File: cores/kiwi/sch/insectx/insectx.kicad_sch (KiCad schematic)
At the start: 0 parts

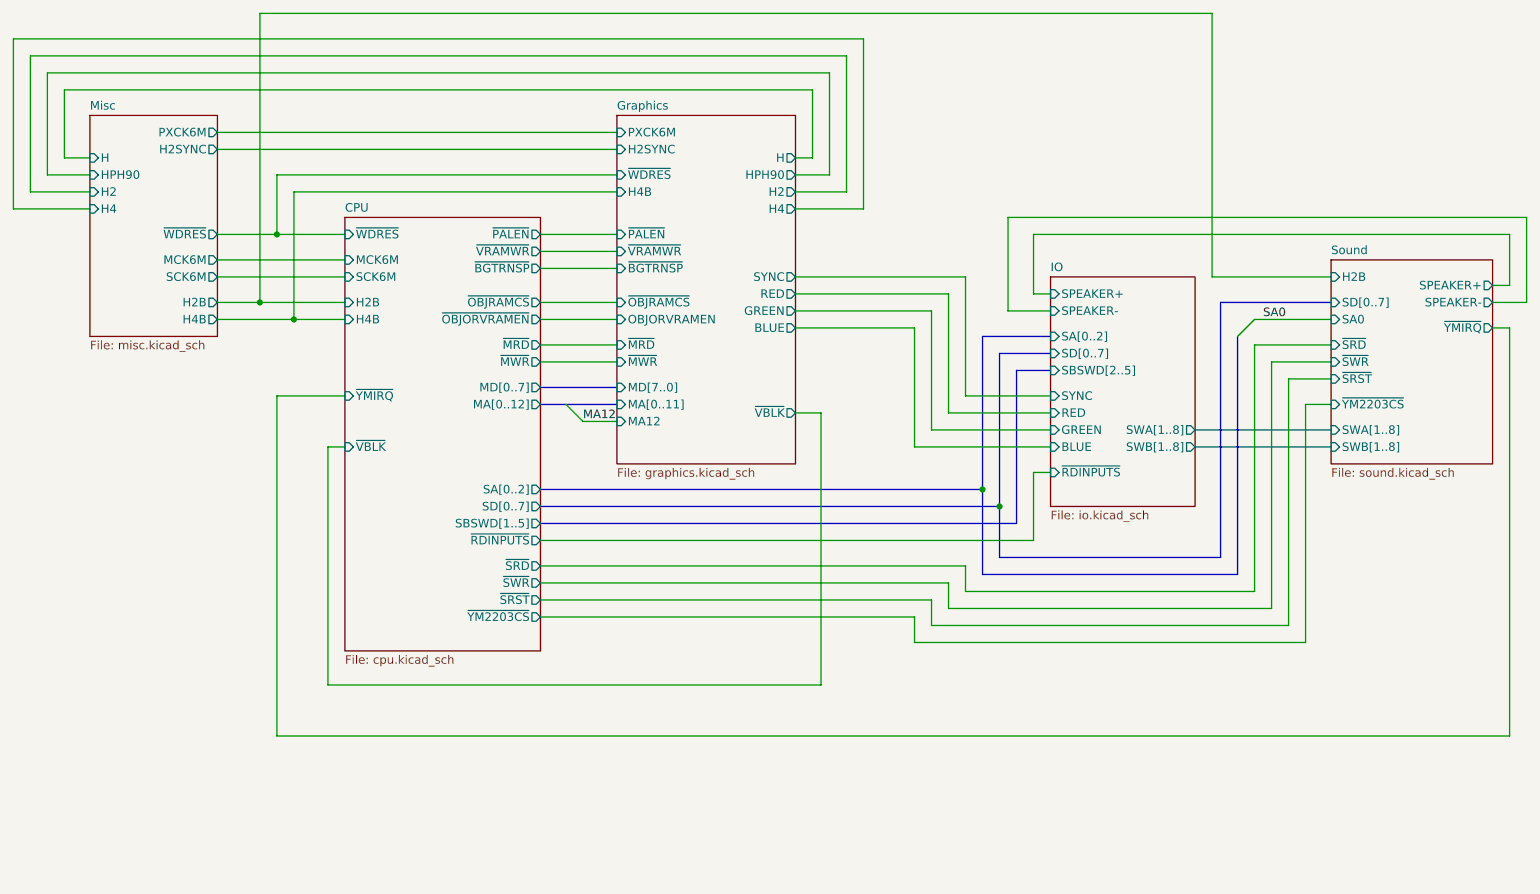
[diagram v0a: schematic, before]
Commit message: Updated schematics according to: [insectx] schematic signals #22
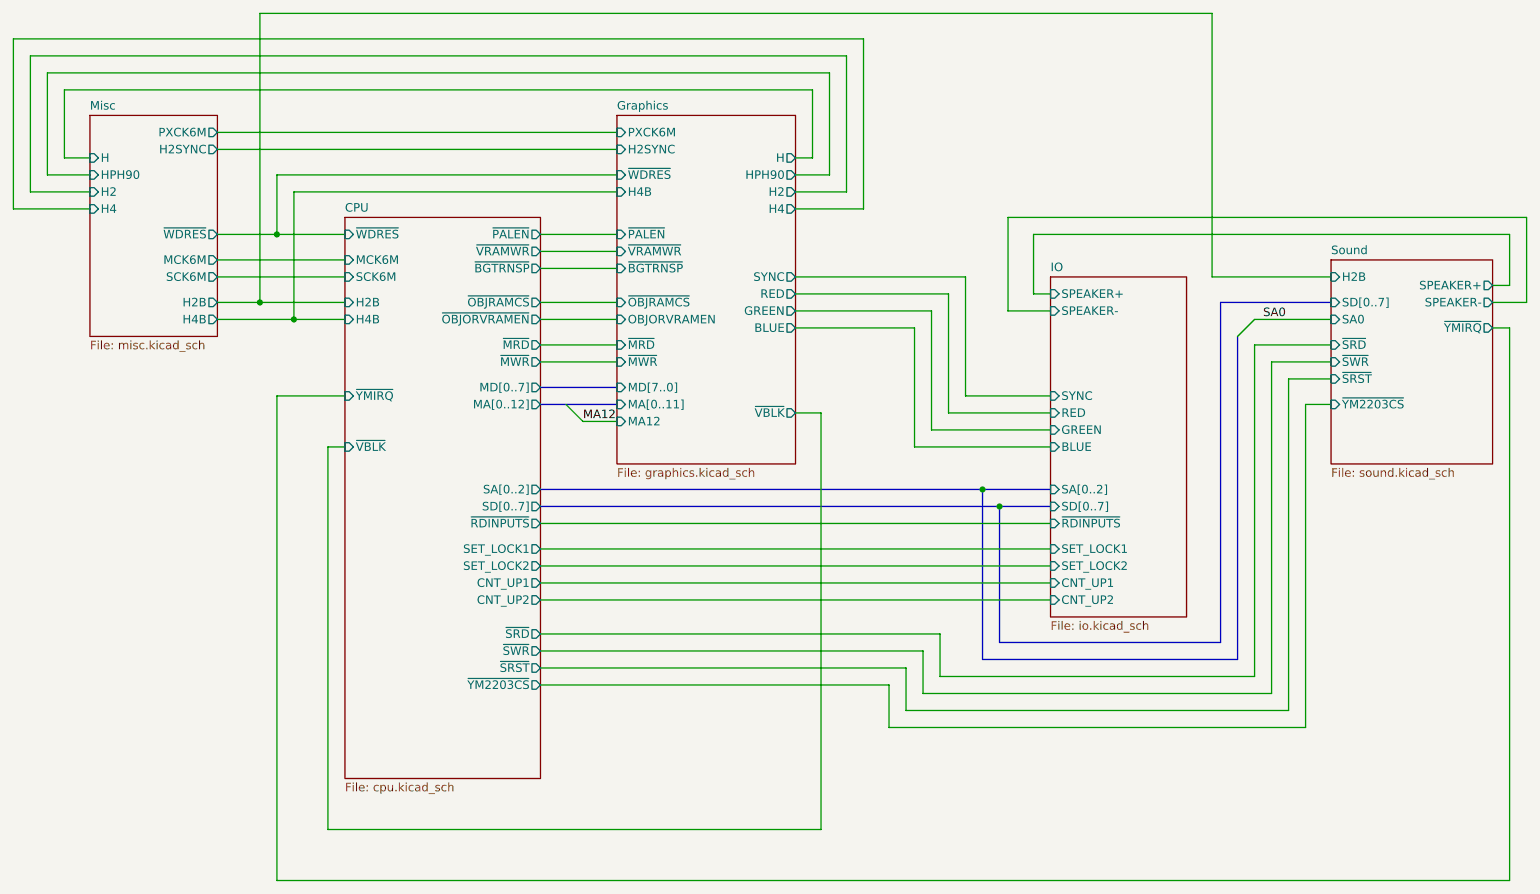
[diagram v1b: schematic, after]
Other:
- sheet CPU ports: added CNT_UP1, CNT_UP2, SET_LOCK1, SET_LOCK2; removed SBSWD[1..5]
- sheet IO ports: added CNT_UP1, CNT_UP2, SET_LOCK1, SET_LOCK2; removed SBSWD[2..5], SWA[1..8], SWB[1..8]
- sheet Sound ports: added none; removed SWA[1..8], SWB[1..8]
